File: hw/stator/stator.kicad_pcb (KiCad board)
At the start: 12 copper layers, 175 x 175 mm, 1 part

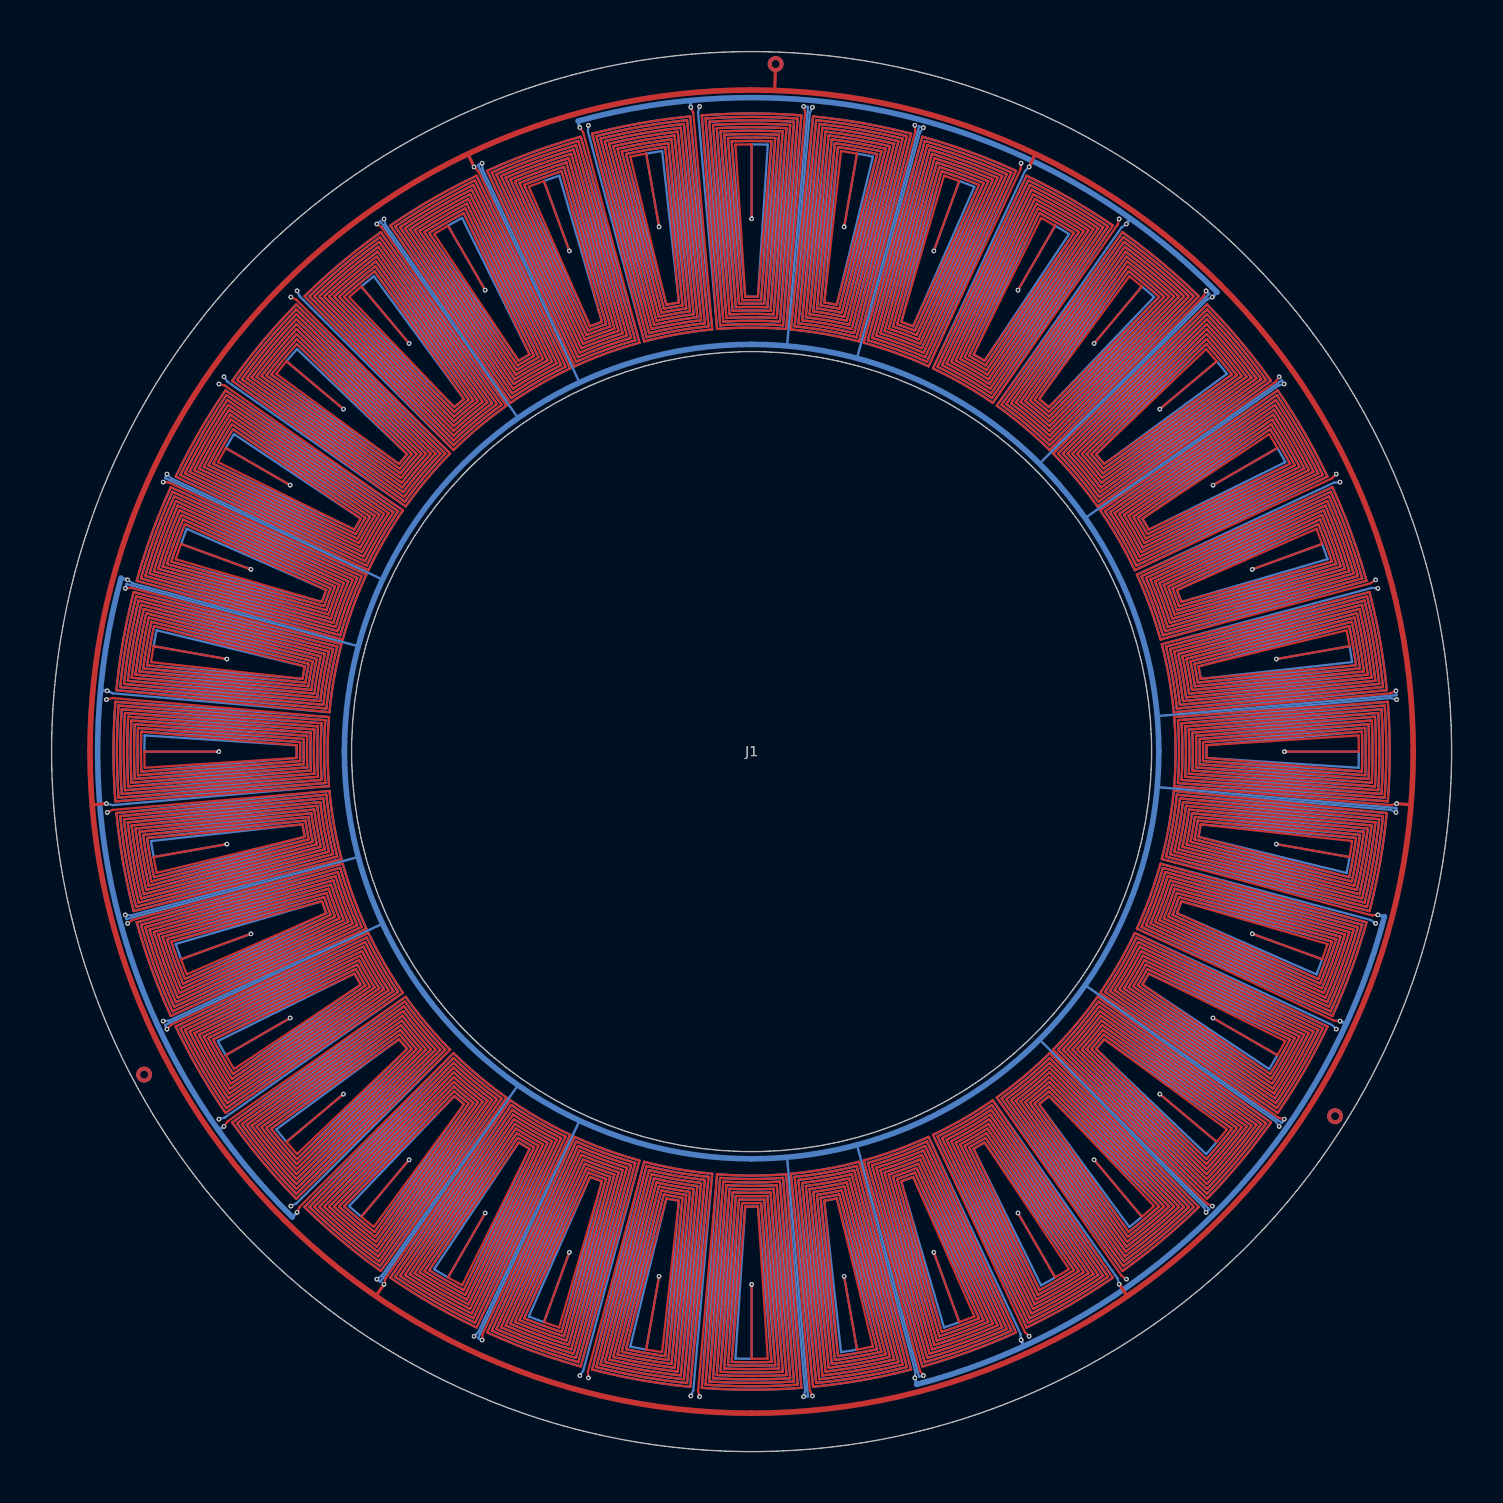
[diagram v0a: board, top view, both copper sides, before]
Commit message: Round 9 in progress: stator layout v2 (coils to r 84.6, +14 % torque), N-S rotor comparison, base as cheap parts, BOM at 20 and 100 units
Co-Authored-By: Claude Fable 5.1 <noreply@anthropic.com>
Claude-Session: https://claude.ai/code/session_01RhbB1sts16H7Chkqp6ycKd
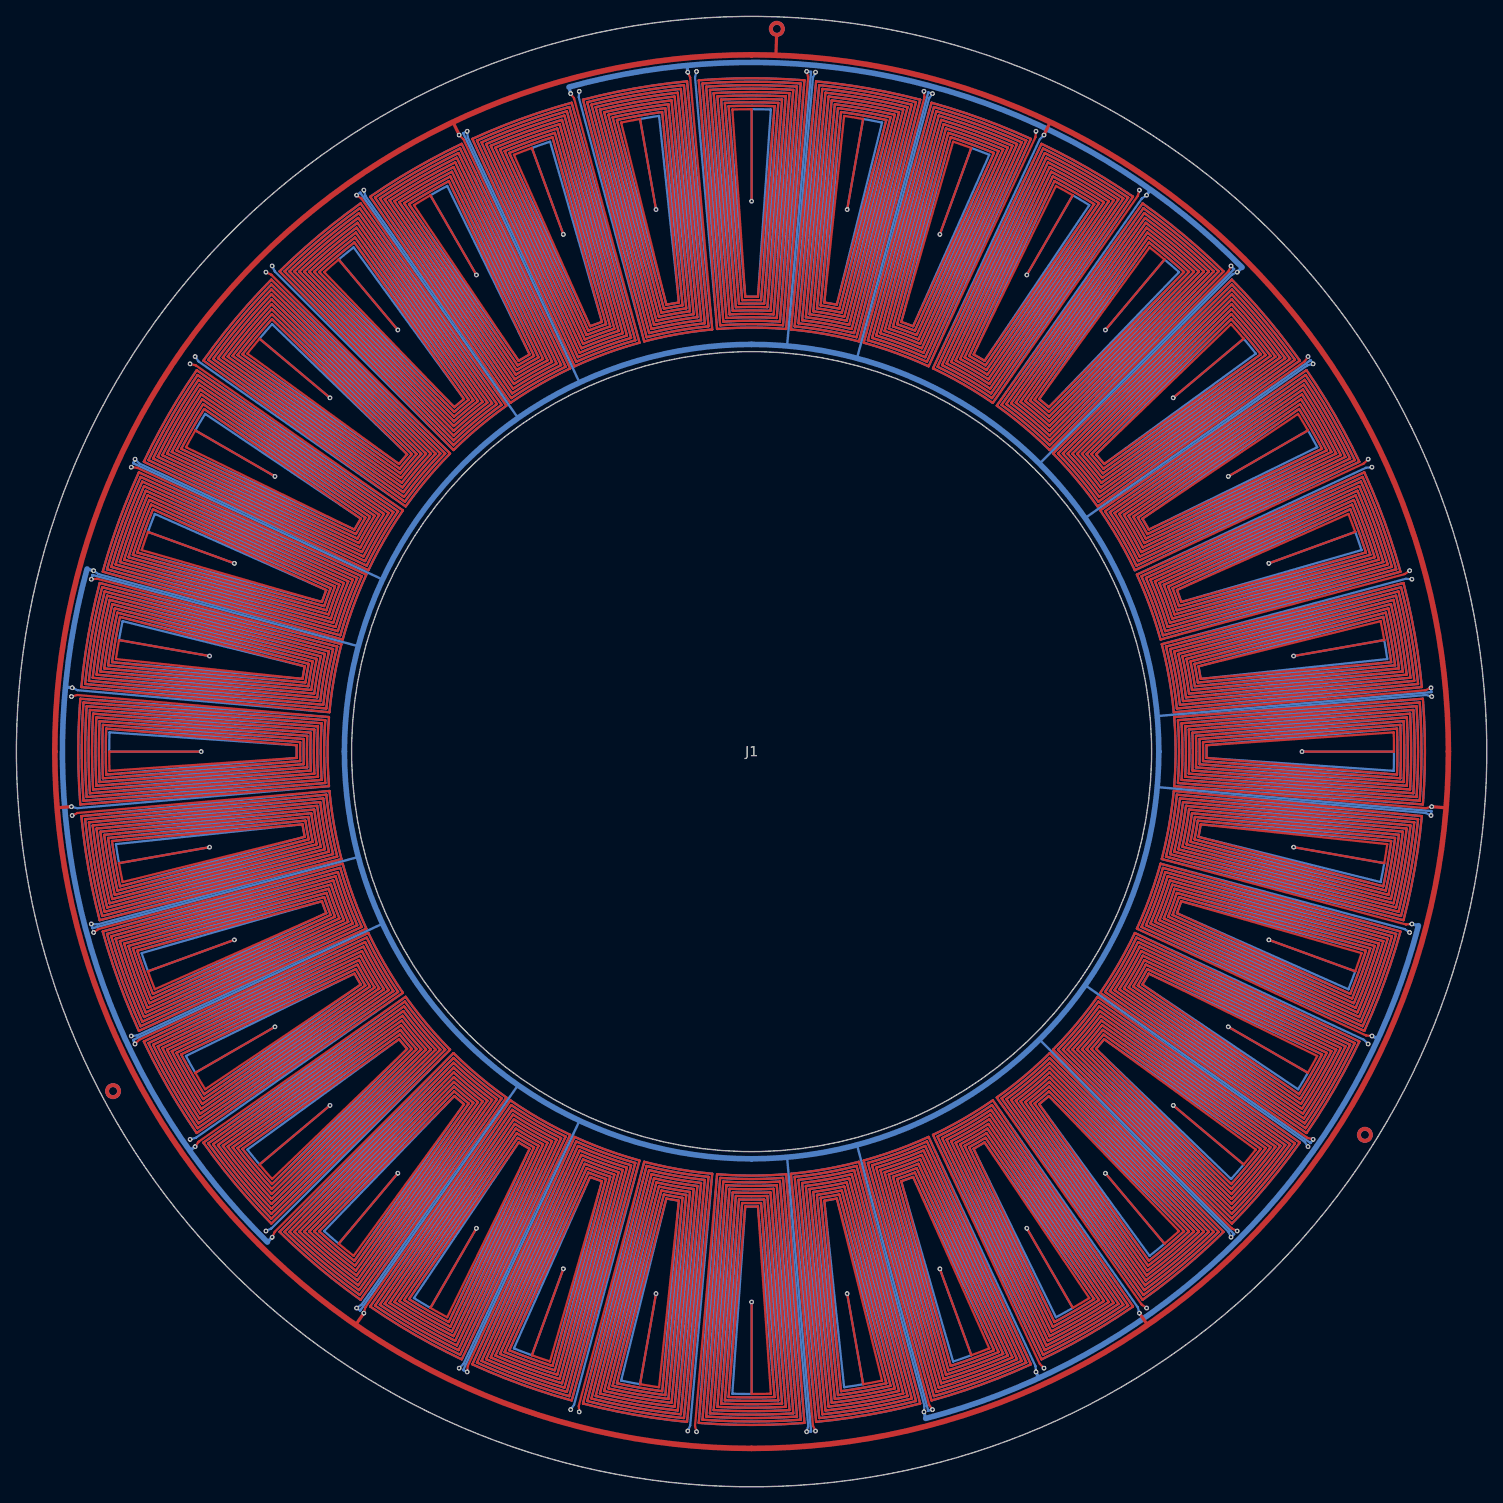
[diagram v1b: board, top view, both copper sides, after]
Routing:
- net (no net): track 269272.0 -> 311934.9 mm
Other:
- board size 175 x 175 mm -> 183.8 x 183.8 mm
